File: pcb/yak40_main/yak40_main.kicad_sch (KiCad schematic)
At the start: 139 parts, among them J1 Conn_01x04, J2 Conn_01x03_Pin, SW1 SW_Push, SW10 SW_Push, SW11 SW_Push, SW12 SW_Push, SW13 SW_Push, SW14 SW_Push, SW15 SW_Push, SW16 SW_Push, SW17 SW_Push, SW18 SW_Push, SW19 SW_Push, SW2 SW_Push, SW20 SW_Push, SW21 SW_Push, SW22 SW_Push, SW23 SW_Push, SW24 SW_Push, SW25 SW_Push, SW26 SW_Push, SW27 SW_Push, SW28 SW_Push, SW29 SW_Push, SW3 SW_Push, SW30 SW_Push, SW31 SW_Push, SW32 SW_Push, SW33 SW_Push, SW34 SW_Push, SW35 SW_Push, SW36 SW_Push, SW37 SW_Push, SW38 SW_Push, SW39 SW_Push, SW4 SW_Push, SW40 SW_Push, SW41 SW_Push, SW42 SW_Push, SW43 SW_Push, SW44 SW_Push, SW45 SW_Push, SW46 SW_Push, SW47 SW_Push, SW48 SW_Push, SW49 SW_Push, SW5 SW_Push, SW50 SW_Push, SW51 SW_Push, SW52 SW_Push, SW53 SW_Push, SW54 SW_Push, SW55 SW_Push, SW6 SW_Push, SW7 SW_Push, SW8 SW_Push, SW9 SW_Push, U1 NCP1117-3.3_SOT223, U2 RP2040, U3 W25Q128JVS, Y1 Crystal

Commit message: Update pcb
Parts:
- removed D14, D40, D41: DIODE, Diode_SMD:D_1206_3216Metric_Pad1.42x1.75mm_HandSolder, symbol Diode:1N4148W
- removed U1: NCP1117-3.3_SOT223, Package_TO_SOT_SMD:SOT-223-3_TabPin2, symbol Regulator_Linear:NCP1117-3.3_SOT223
- removed Y1: Crystal, Crystal:Resonator_SMD_Murata_CSTxExxV-3Pin_3.0x1.1mm_HandSoldering, symbol Device:Crystal_GND2
- added C17, C18: 22p, Capacitor_SMD:C_0402_1005Metric, symbol Device:C_Small
- added U1: XC6206PxxxMR, Package_TO_SOT_SMD:SOT-23-3, symbol Regulator_Linear:XC6206PxxxMR
- added Y1: 12MHz, Crystal:Crystal_SMD_3225-4Pin_3.2x2.5mm, symbol Device:Crystal_GND24_Small
- C10, C9: value 10u -> 1u
- D1, D10, D11, D12, D13, D15, D16, D17, D18, D19, D2, D20, D21, D22, D23, D24, D25, D26, D27, D28, D29, D3, D30, D31, D32, D33, D34, D35, D36, D37, D38, D39, D4, D42, D43, D44, D45, D46, D47, D48, D49, D5, D6, D7, D8, D9: footprint Diode_SMD:D_1206_3216Metric_Pad1.42x1.75mm_HandSolder -> Diode_SMD:D_SOD-123
- R6: LCSC (none) -> C11702
- SW54, SW55: footprint Button_Switch_SMD:SW_Push_1P1T_NO_Vertical_Wuerth_434133025816 -> Button_Switch_SMD:SW_Push_1P1T_XKB_TS-1187A
- U3: footprint Package_SON:WSON-8-1EP_6x5mm_P1.27mm_EP3.4x4.3mm -> Package_SO:SOIC-8_5.23x5.23mm_P1.27mm
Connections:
- net +3V3: now also U1.2 (VO)
- net +5V: now also U1.3 (VI)
- net GND: now also C17.1, C18.1, U1.1 (GND), Y1.2, Y1.4
- net XIN: now also C17.2, Y1.3
- net XOUT: now also R6.2; no longer R6.1
- new net XTAL_O: C18.2, R6.1, Y1.1

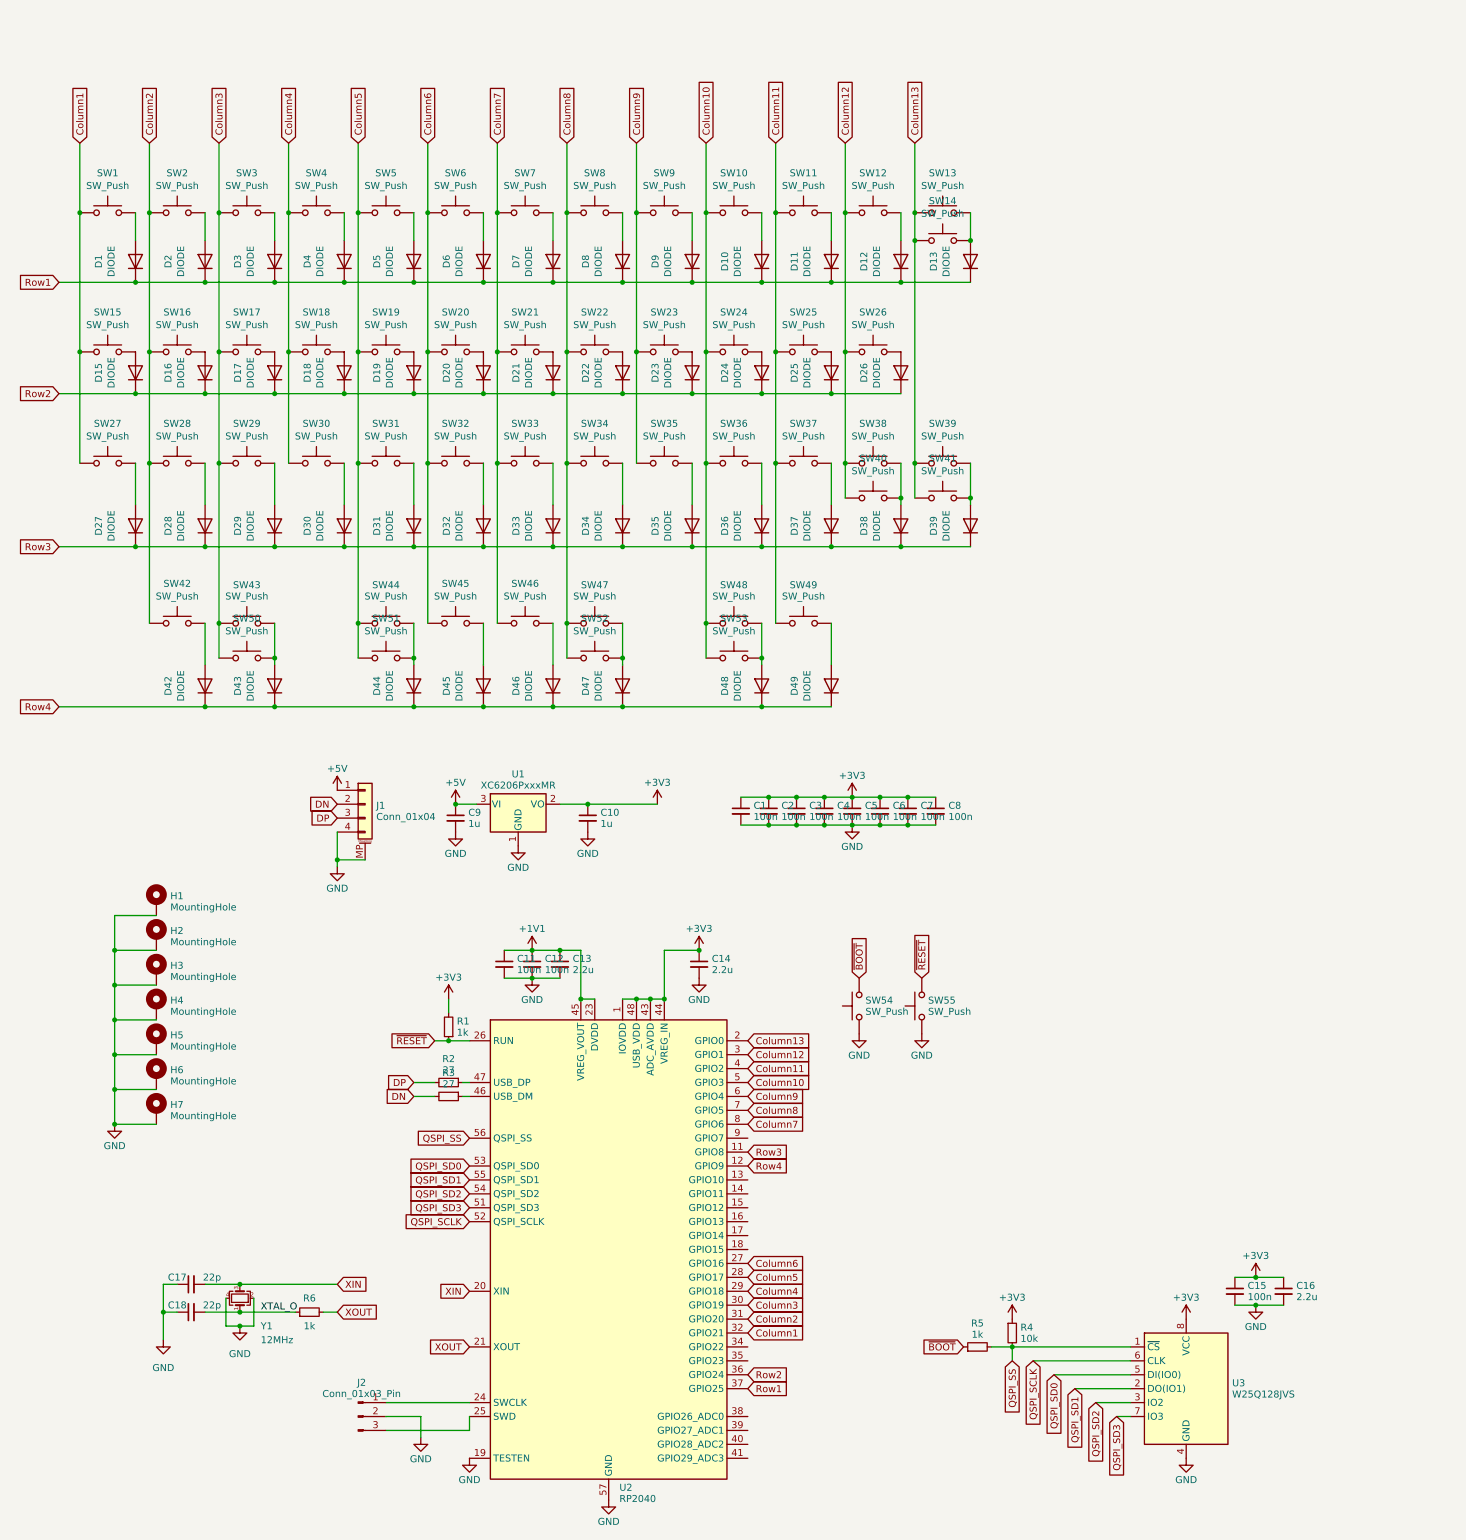
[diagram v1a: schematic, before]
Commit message: Support LED and rotary encoders
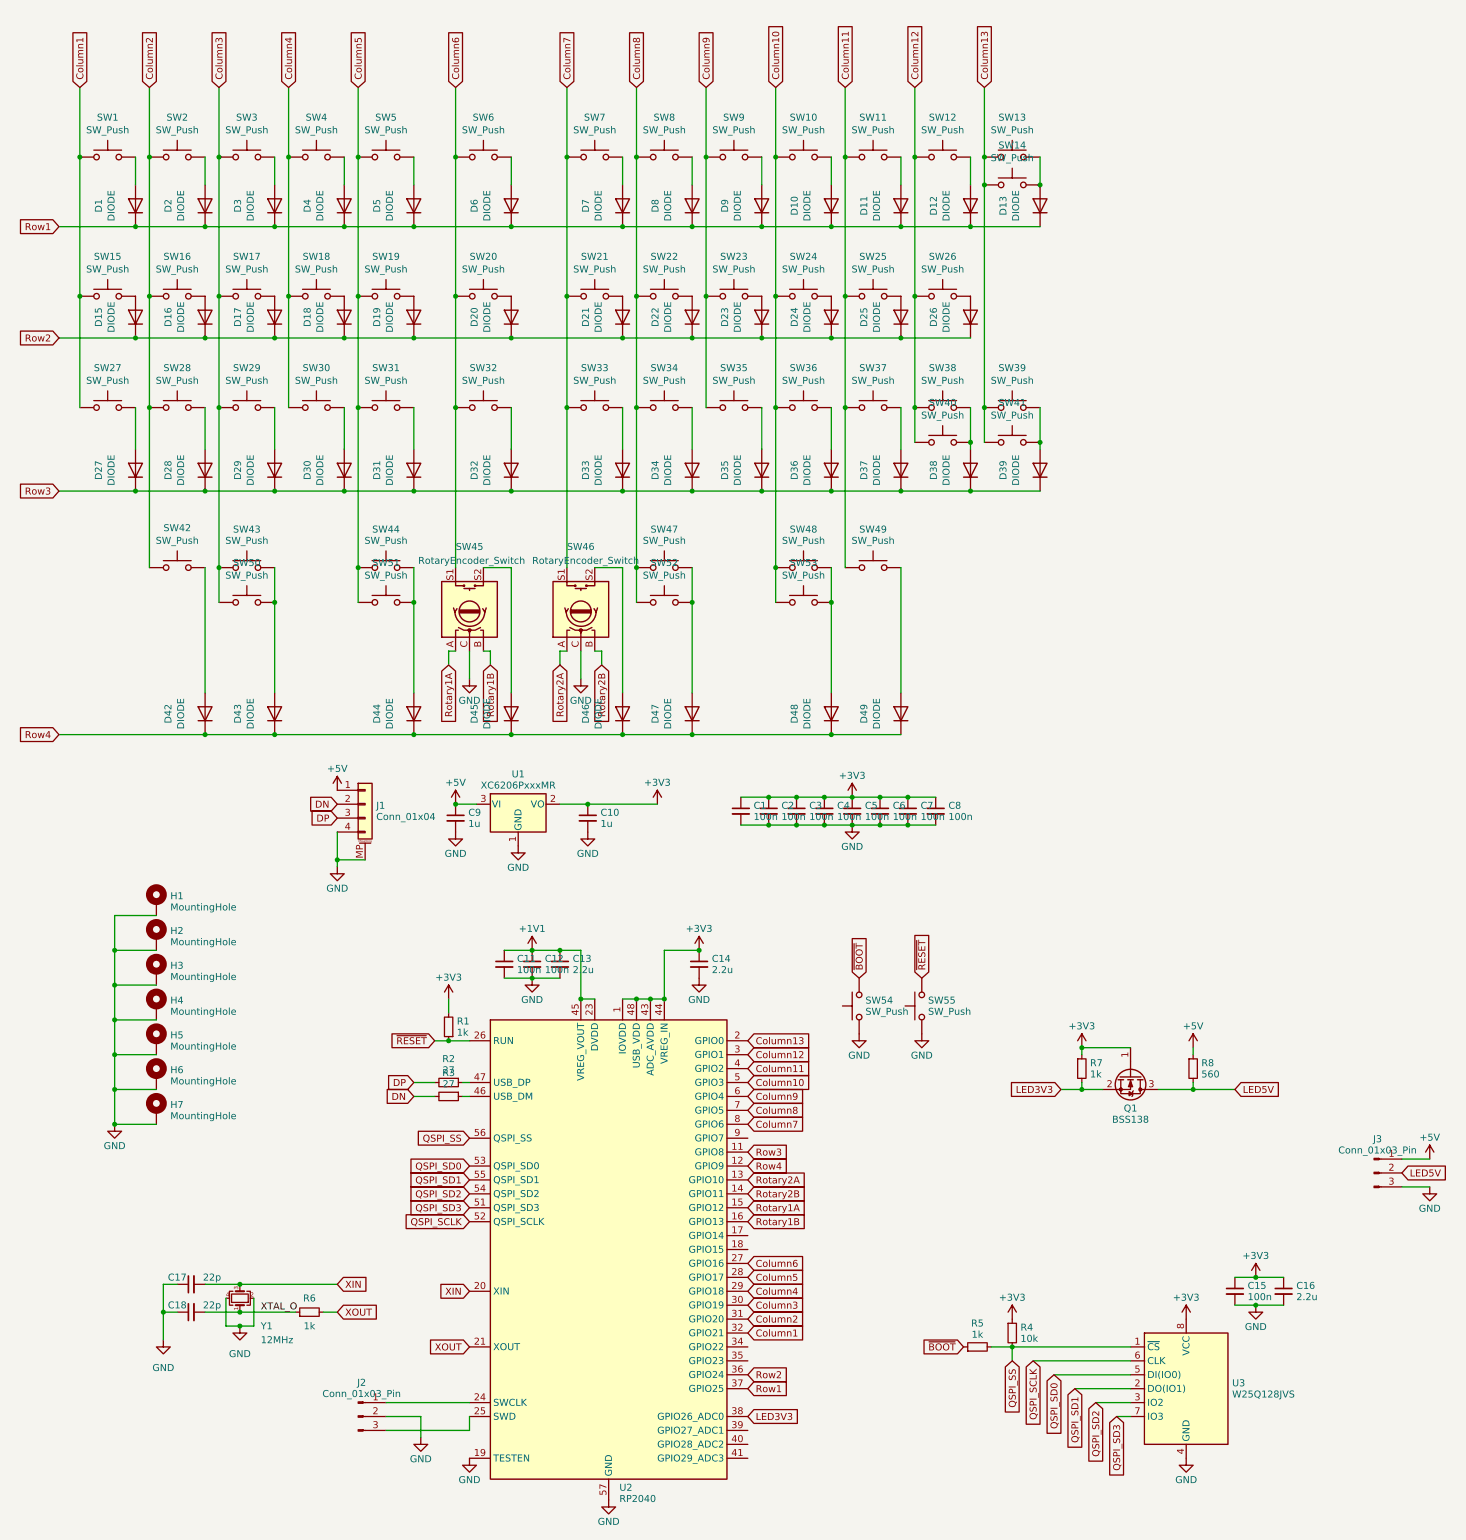
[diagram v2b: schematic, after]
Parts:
- removed SW45, SW46: SW_Push, MX_Hotswap:MX-Hotswap-1U, symbol Switch:SW_Push
- added J3: Conn_01x03_Pin, Connector_PinHeader_2.54mm:PinHeader_1x03_P2.54mm_Vertical, symbol Connector:Conn_01x03_Pin
- added Q1: BSS138, Package_TO_SOT_SMD:SOT-23, symbol Transistor_FET:BSS138
- added R7: 1k, Resistor_SMD:R_0402_1005Metric, symbol Device:R_Small
- added R8: 560, Resistor_SMD:R_0603_1608Metric, symbol Device:R_Small
- added SW45, SW46: RotaryEncoder_Switch, kicad-libs:SW_Cherry_MX_1.00u_Kailh_EC12, symbol Device:RotaryEncoder_Switch
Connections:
- net +3V3: now also Q1.1 (G), R7.1
- net +5V: now also J3.1 (Pin_1), R8.1
- net Column6: now also SW45.S1
- net Column7: now also SW46.S1
- net GND: now also J3.3 (Pin_3), SW45.C, SW46.C
- net at D46.2 (A): now also SW46.S2
- net Rotary2A: now reaches U2.13 (GPIO10)
- net Rotary2A: now also SW46.A
- net Rotary2B: now reaches U2.14 (GPIO11)
- net Rotary2B: now also SW46.B
- net Rotary1A: now reaches U2.15 (GPIO12)
- net Rotary1A: now also SW45.A
- net Rotary1B: now reaches U2.16 (GPIO13)
- net Rotary1B: now also SW45.B
- net LED3V3: now reaches U2.38 (GPIO26_ADC0)
- net LED3V3: now also Q1.2 (S), R7.2
- net at D45.2 (A): now also SW45.S2
- new net LED5V: J3.2 (Pin_2), Q1.3 (D), R8.2
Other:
- moved on the sheet: D1, D10, D11, D12, D13, D15, D16, D17, D18, D19, D2, D20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
